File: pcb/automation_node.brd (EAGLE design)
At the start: 107.1 x 77.8 mm, 27 parts, among them IC1 POWER_FET, IC2 POWER_FET, IC3 POWER_FET, IC4 POWER_FET, IC5 POWER_FET, IC6 FEATHER-ESP32, J1 POWER-VIAS, J2 POWER-VIAS, J3 POWER-VIAS, J4 POWER-VIAS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

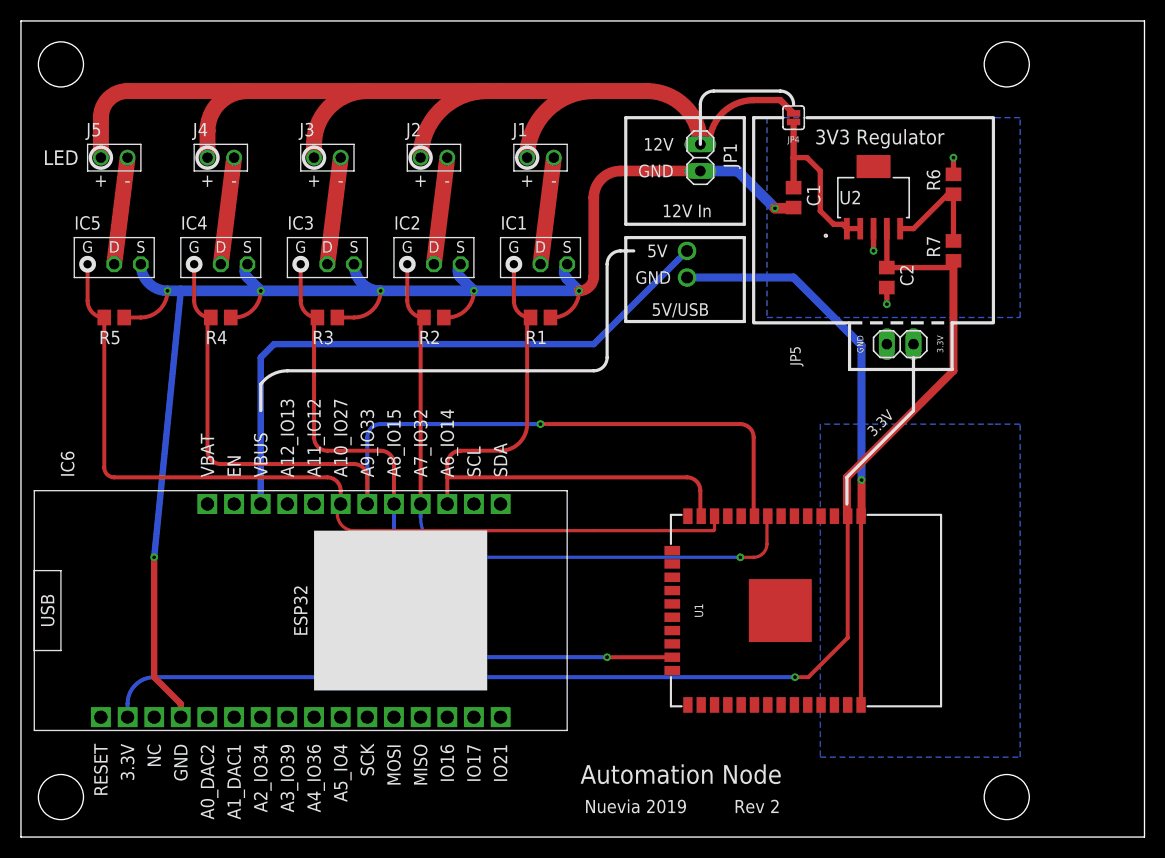
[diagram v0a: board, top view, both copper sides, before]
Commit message: added RFM69, finished routing all but RFM69
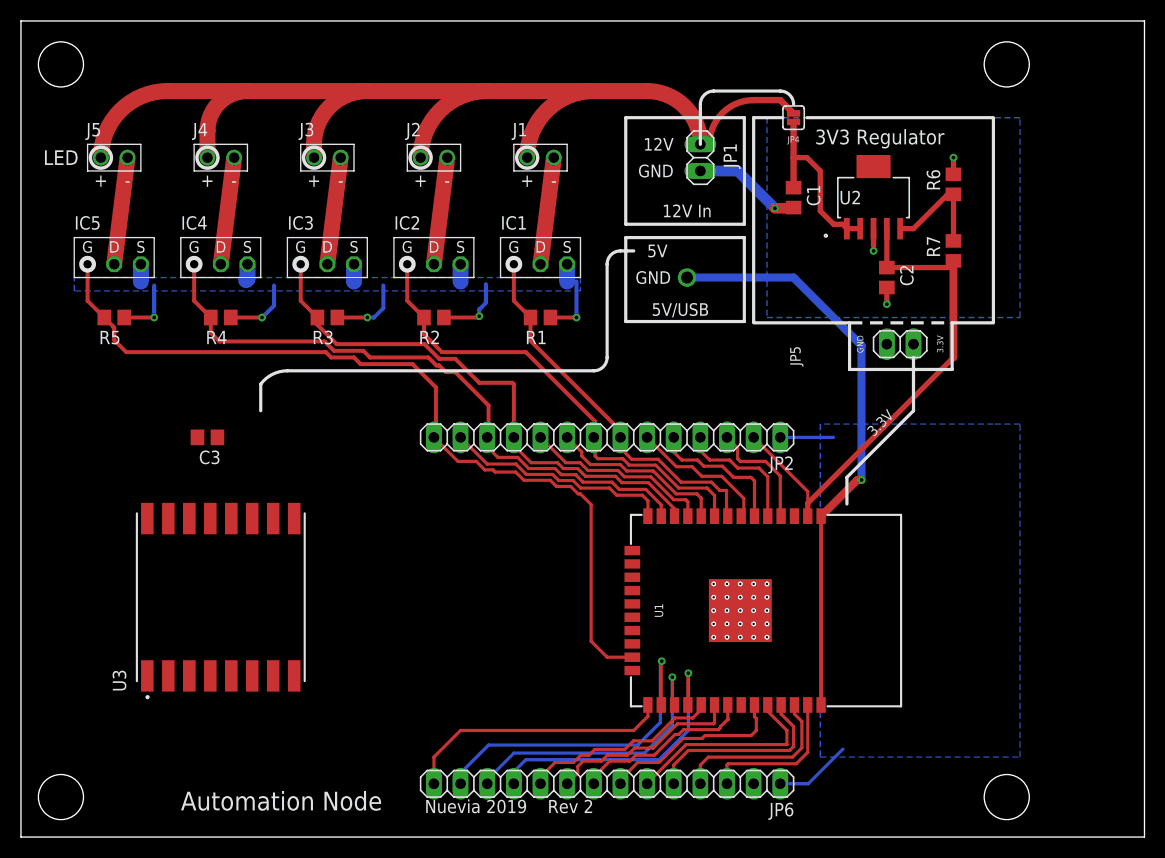
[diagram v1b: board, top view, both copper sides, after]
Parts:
- removed IC6: FEATHER-ESP32, VCO-Eagle_parts:ESP32_FEATHER
- added C3: 100uF, rcl:C0805
- added JP6: (no value), pinhead:1X14
- added U3: RFM69HCW, VanEagleLib:MOD_COM-13909
- JP2: value PROTO_VIA_COMPACT -> (none); device VanEagleLib:PROTO_VIA -> pinhead:1X14
- moved JP2 19.3 mm to (55.9, 38.1), turned to 180 degrees
- moved U1 3.81 mm to (68.6, 21.6)
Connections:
- removed net +5V: IC6.VBUS, JP2.1
- new net ADC1: JP2.3, U1.4
- new net ADC2: JP2.4, U1.5
- new net ADC3: JP2.5, U1.6
- new net ADC4: JP2.6, U1.7
- new net ANT: U3.9
- new net GPIO0: JP6.14, U1.25
- new net IO12: JP2.13, U1.14
- new net IO16: JP6.12, U1.27
- new net IO17: JP6.11, U1.28
- new net IO25: JP2.9, U1.10
- new net IO26: JP2.10, U1.11
- new net MISO: JP6.8, U1.31, U3.2
- new net MOSI: JP6.3, U1.37, U3.3
- new net RFM69_IRQ: JP6.13, U1.26, U3.14
- new net RFM69_RS: U3.6
- new net RFM69_SS: JP6.10, U1.29, U3.5
- new net RX: JP6.6, U1.34
- new net SCK: JP6.9, U1.30, U3.4
- new net SCL: JP6.4, U1.36
- new net SDA: JP6.7, U1.33
- new net TX: JP6.5, U1.35
- net +3V3: now also C3.1, JP2.2, JP6.2, U3.13; no longer IC6.3.3V
- net GND: now also C3.2, JP2.1, JP6.1, U3.1, U3.10, U3.8; no longer IC6.GND
- net PWM1: now also IC4.1, JP2.12, R4.2; no longer IC1.1, IC6.A6_IO14, R1.2
- net PWM2: now also IC1.1, JP2.7, R1.2; no longer IC2.1, IC6.A7_IO32, R2.2
- net PWM3: now also IC5.1, JP2.14, R5.2; no longer IC3.1, IC6.A8_IO15, R3.2
- net PWM4: now also IC2.1, JP2.8, R2.2; no longer IC4.1, IC6.A9_IO33, R4.2
- net PWM5: now also IC3.1, JP2.11, R3.2; no longer IC5.1, IC6.A10_IO27, R5.2
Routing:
- net GND: track 211.8 -> 126.2 mm, vias 11 -> 10
- net +3V3: track 123.3 -> 50.3 mm, vias 1 -> 0
- net +5V: track 58.8 -> 0.00 mm
- net PWM4: track 89.2 -> 45.6 mm, vias 1 -> 0
- net RFM69_IRQ: track 0.00 -> 32.2 mm, vias 0 -> 1
- net PWM5: track 83.3 -> 52.0 mm
- net IO17: track 0.00 -> 27.9 mm, vias 0 -> 1
- net IO16: track 0.00 -> 27.5 mm, vias 0 -> 1
- net PWM2: track 62.7 -> 36.2 mm, vias 1 -> 0
- net GPIO0: track 0.00 -> 25.6 mm
- net IO12: track 0.00 -> 21.8 mm
- net RX: track 0.00 -> 19.4 mm
- net RFM69_SS: track 0.00 -> 19.1 mm
- net SDA: track 0.00 -> 19.0 mm
- net SCK: track 0.00 -> 18.5 mm
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
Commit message: added programming header for ESP32
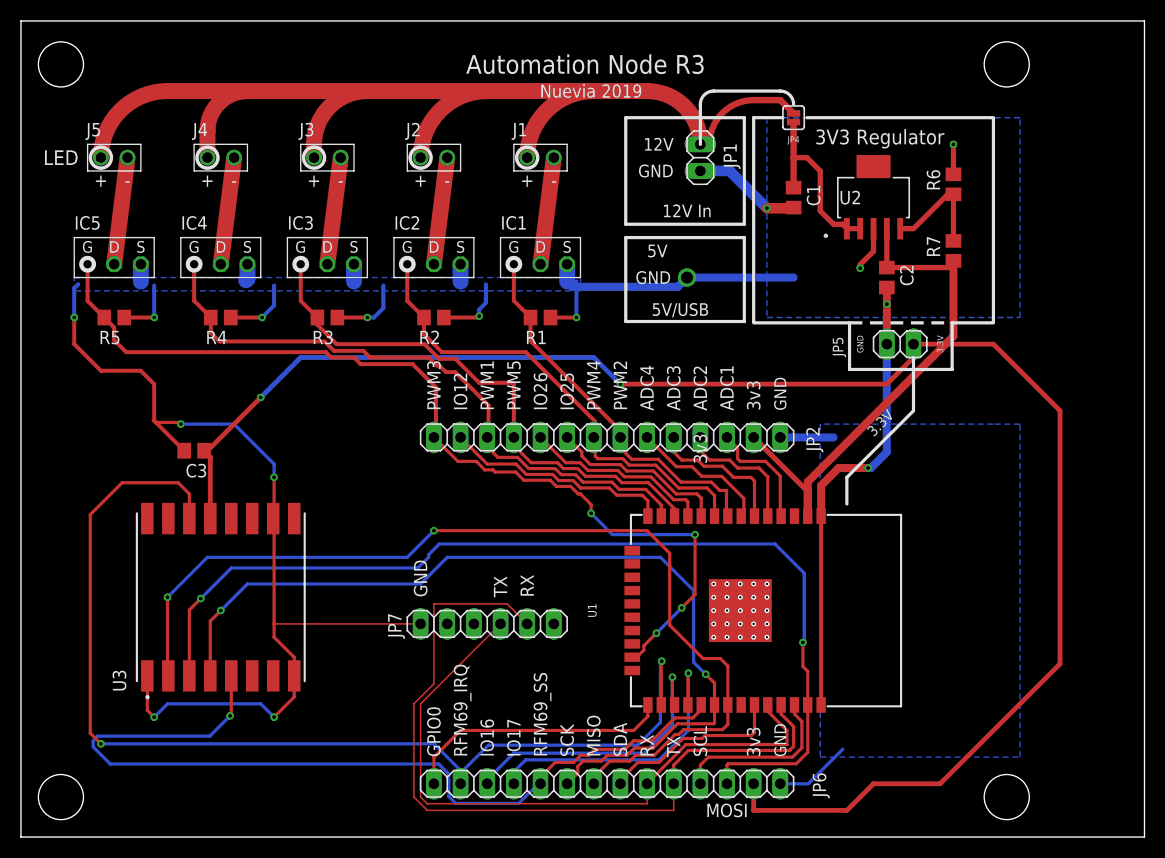
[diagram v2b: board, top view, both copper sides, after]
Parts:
- added JP7: (no value), pinhead:1X06
- moved C3 1.80 mm to (16.5, 36.8)
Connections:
- net GND: now also JP7.1
- net RX: now also JP7.4
- net TX: now also JP7.5
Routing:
- net +3V3: track 50.3 -> 210.0 mm, vias 0 -> 2
- net GND: track 126.2 -> 228.4 mm, vias 10 -> 15
- net MOSI: track 14.5 -> 96.1 mm, vias 0 -> 2
- net MISO: track 17.2 -> 94.0 mm, vias 0 -> 2
- net RFM69_IRQ: track 32.2 -> 104.5 mm, vias 1 -> 2
- net SCK: track 18.5 -> 85.4 mm, vias 0 -> 2
- net RFM69_SS: track 19.1 -> 84.5 mm, vias 0 -> 1
- net TX: track 18.4 -> 75.1 mm
- net RX: track 19.4 -> 62.9 mm
- net PWM3: track 81.0 -> 89.4 mm, vias 0 -> 4
- net SDA: track 19.0 -> 17.6 mm
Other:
- board text added: "3v3"
- board text added: "ADC1"
- board text added: "ADC2"
- board text added: "ADC3"
- board text added: "ADC4"
- board text added: "Automation Node R3"
- board text added: "GPIO0"
- board text added: "IO12"
- board text added: "IO16"
- board text added: "IO17"
- board text added: "IO25"
- board text added: "IO26"
- board text added: "MISO"
- board text added: "MOSI"
- board text added: "PWM1"
- board text added: "PWM2"
- board text added: "PWM3"
- board text added: "PWM4"
- board text added: "PWM5"
- board text added: "RFM69_IRQ"
- board text added: "RFM69_SS"
- board text added: "RX"
- board text added: "SCK"
- board text added: "SCL"
- board text added: "SDA"
- board text added: "TX"
- board text removed: "Automation Node"
- board text removed: "Rev 2"

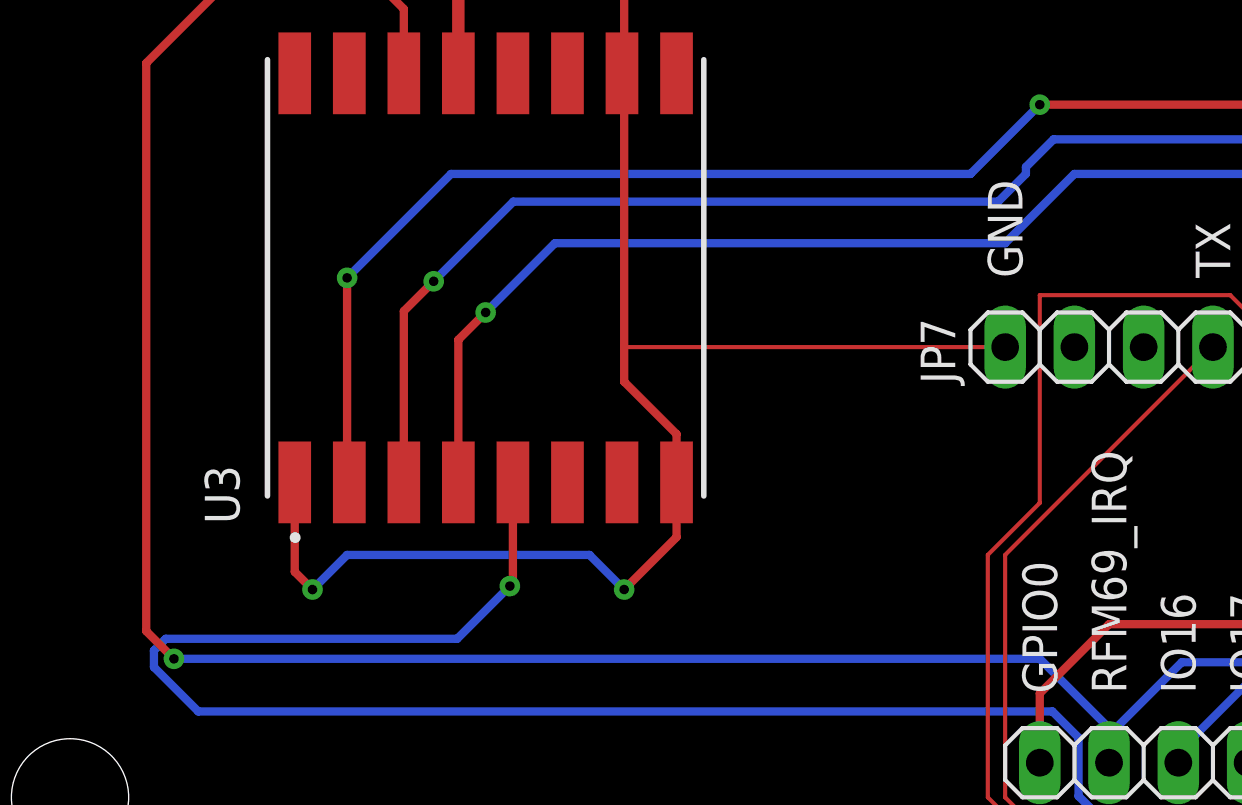
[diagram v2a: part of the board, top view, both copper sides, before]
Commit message: moved vias away from bottom side of rfm69
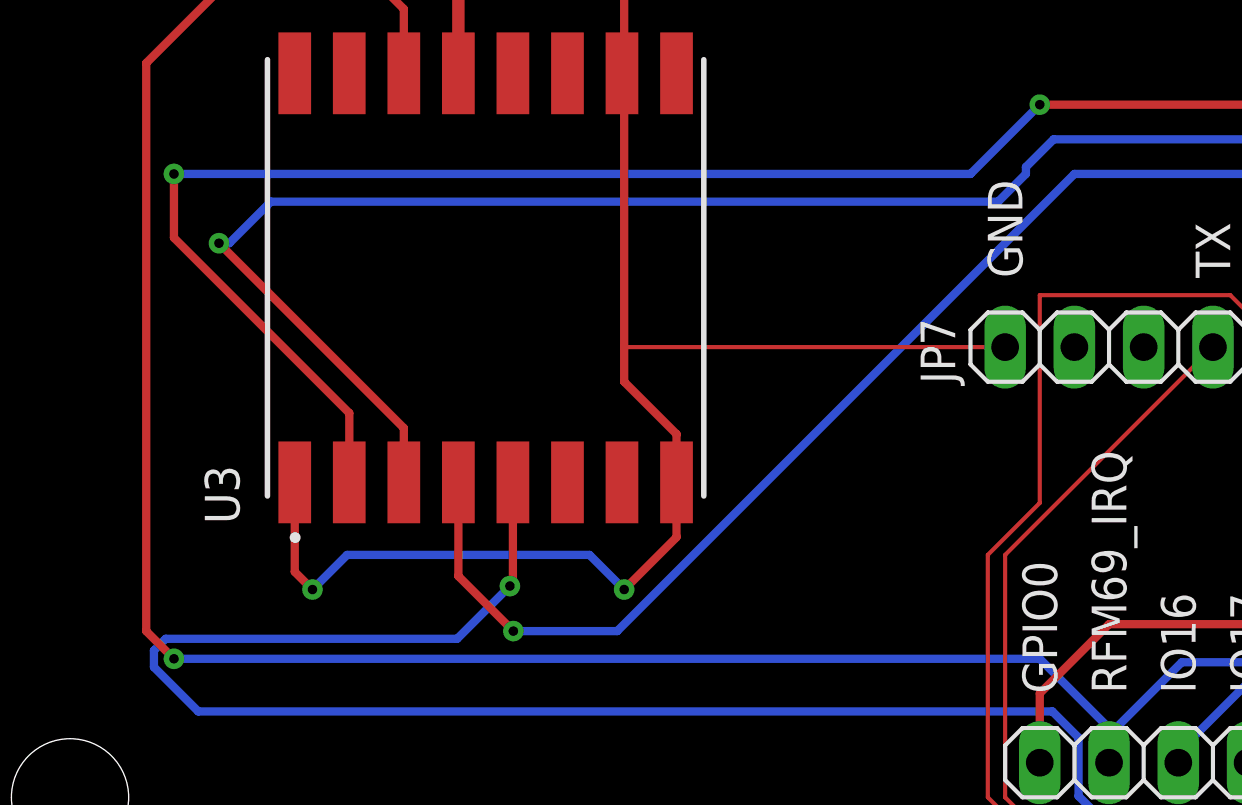
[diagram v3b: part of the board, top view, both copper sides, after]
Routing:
- net MISO: track 94.0 -> 105.2 mm
- net MOSI: track 96.1 -> 107.2 mm
- net SCK: track 85.4 -> 88.9 mm
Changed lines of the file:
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@@
 <setting verticaltext="up"/>
 </settings>
-<grid distance="50" unitdist="mil" unit="mil" style="lines" multiple="1" display="no" altdistance="5" altunitdist="mil" altunit="mil"/>
+<grid distance="50" unitdist="mil" unit="mm" style="lines" multiple="1" display="no" altdistance="5" altunitdist="mil" altunit="mil"/>
 <layers>
 <layer number="1" name="Top" color="4" fill="1" visible="yes" active="yes"/>
@@
 <wire x1="55.90253125" y1="7.7978" x2="57.80753125" y2="7.7978" width="0.3048" layer="1"/>
 <wire x1="58.49333125" y1="8.4836" x2="60.27133125" y2="8.4836" width="0.3048" layer="1"/>
-<wire x1="18.05" y1="15.36" x2="18.05" y2="20.59" width="0.3048" layer="1"/>
-<wire x1="18.05" y1="20.59" x2="19.05" y2="21.59" width="0.3048" layer="1"/>
-<via x="19.05" y="21.59" extent="1-16" drill="0.35"/>
-<wire x1="19.05" y1="21.59" x2="21.59" y2="24.13" width="0.3048" layer="16"/>
-<wire x1="21.59" y1="24.13" x2="38.1" y2="24.13" width="0.3048" layer="16"/>
-<wire x1="38.1" y1="24.13" x2="40.64" y2="26.67" width="0.3048" layer="16"/>
+<wire x1="20.066" y1="9.906" x2="18.05" y2="11.922" width="0.3048" layer="1"/>
+<wire x1="18.05" y1="15.36" x2="18.05" y2="11.922" width="0.3048" layer="1"/>
+<via x="20.066" y="9.906" extent="1-16" drill="0.35"/>
+<wire x1="40.64" y1="26.67" x2="23.876" y2="9.906" width="0.3048" layer="16"/>
+<wire x1="20.066" y1="9.906" x2="23.876" y2="9.906" width="0.3048" layer="16"/>
 <wire x1="40.64" y1="26.67" x2="60.96" y2="26.67" width="0.3048" layer="16"/>
 <wire x1="64.135" y1="16.6652" x2="65.278" y2="15.5222" width="0.3048" layer="16"/>
@@
 <wire x1="67.31" y1="6.858" x2="67.31" y2="5.08" width="0.3048" layer="1"/>
 <wire x1="75.01" y1="8.081" x2="73.914" y2="6.985" width="0.3048" layer="1"/>
-<wire x1="16.05" y1="15.36" x2="16.05" y2="21.638" width="0.3048" layer="1"/>
-<wire x1="16.05" y1="21.638" x2="17.145" y2="22.733" width="0.3048" layer="1"/>
-<via x="17.145" y="22.733" extent="1-16" drill="0.35"/>
-<wire x1="17.145" y1="22.733" x2="20.066" y2="25.654" width="0.3048" layer="16"/>
-<wire x1="20.066" y1="25.654" x2="37.846" y2="25.654" width="0.3048" layer="16"/>
+<wire x1="16.05" y1="15.36" x2="16.05" y2="17.351" width="0.3048" layer="1"/>
+<wire x1="16.05" y1="17.351" x2="9.271" y2="24.13" width="0.3048" layer="1"/>
+<via x="9.271" y="24.13" extent="1-16" drill="0.35"/>
+<wire x1="11.176" y1="25.654" x2="9.652" y2="24.13" width="0.3048" layer="16"/>
+<wire x1="9.271" y1="24.13" x2="9.652" y2="24.13" width="0.3048" layer="16"/>
+<wire x1="11.176" y1="25.654" x2="37.846" y2="25.654" width="0.3048" layer="16"/>
 <wire x1="37.846" y1="25.654" x2="38.862" y2="26.67" width="0.3048" layer="16"/>
 <wire x1="38.862" y1="26.67" x2="38.862" y2="26.924" width="0.3048" layer="16"/>
@@
 <wire x1="60.3758" y1="7.7978" x2="58.5978" y2="7.7978" width="0.3048" layer="1"/>
 <wire x1="58.5978" y1="7.7978" x2="58.039" y2="7.239" width="0.3048" layer="1"/>
-<wire x1="14.05" y1="15.36" x2="13.97" y2="15.44" width="0.3048" layer="1"/>
-<wire x1="13.97" y1="15.44" x2="13.97" y2="22.86" width="0.3048" layer="1"/>
-<via x="13.97" y="22.86" extent="1-16" drill="0.35"/>
-<wire x1="13.97" y1="22.86" x2="17.78" y2="26.67" width="0.3048" layer="16"/>
-<wire x1="17.78" y1="26.67" x2="36.83" y2="26.67" width="0.3048" layer="16"/>
+<wire x1="14.05" y1="15.36" x2="14.05" y2="17.9" width="0.3048" layer="1"/>
+<wire x1="7.62" y1="26.67" x2="7.62" y2="24.33" width="0.3048" layer="1"/>
+<wire x1="14.05" y1="17.9" x2="7.62" y2="24.33" width="0.3048" layer="1"/>
+<via x="7.62" y="26.67" extent="1-16" drill="0.35"/>
+<wire x1="7.62" y1="26.67" x2="36.83" y2="26.67" width="0.3048" layer="16"/>
 <wire x1="36.83" y1="26.67" x2="39.37" y2="29.21" width="0.3048" layer="16"/>
 <wire x1="39.37" y1="29.21" x2="59.69" y2="29.21" width="0.3048" layer="1"/>

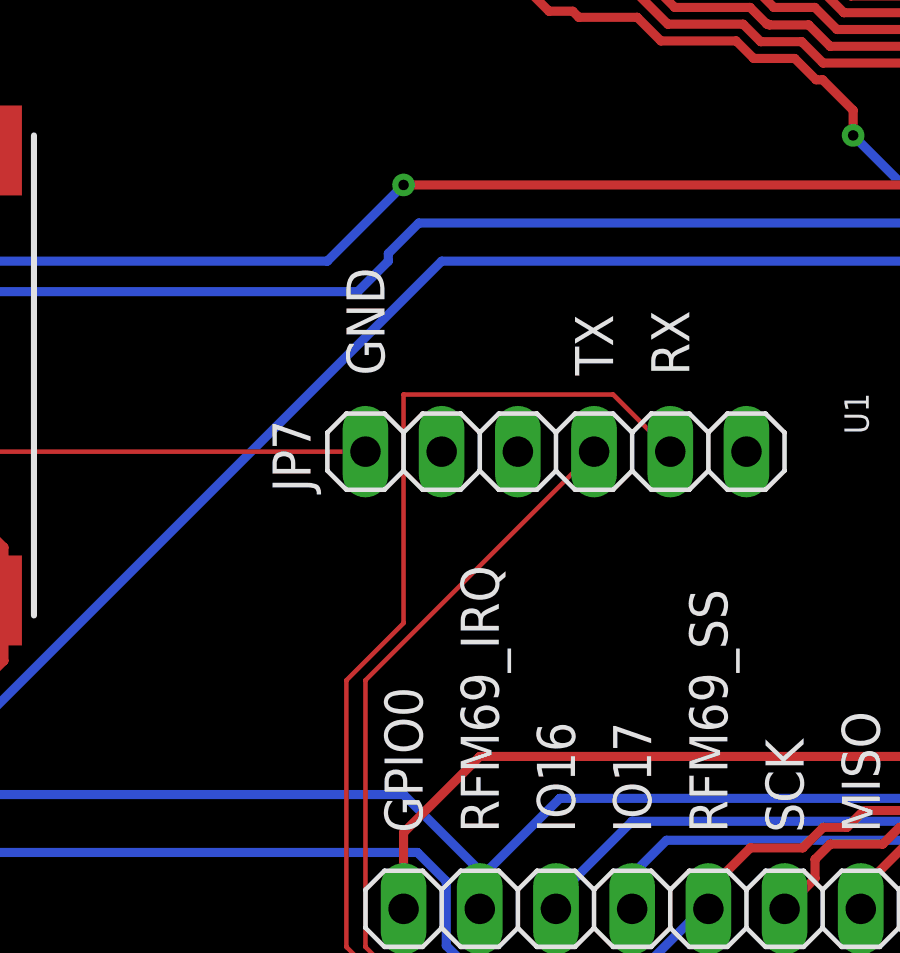
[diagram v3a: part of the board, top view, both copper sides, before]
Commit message: added GPIO0 to programming header
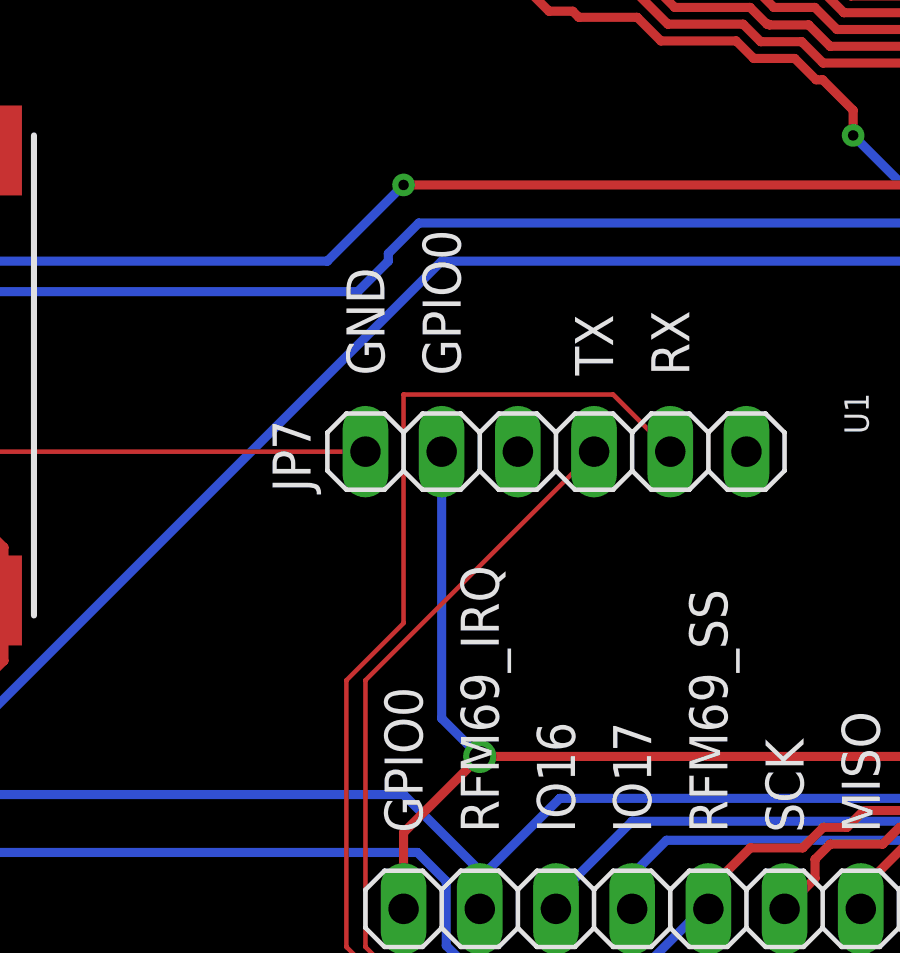
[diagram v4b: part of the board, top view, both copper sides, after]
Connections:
- net GPIO0: now also JP7.2
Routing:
- net GPIO0: track 25.6 -> 36.3 mm, vias 0 -> 1
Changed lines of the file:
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@@
 <text x="48.26" y="22.86" size="1.27" layer="21" rot="R270" align="center-right">RX</text>
 <text x="45.72" y="22.86" size="1.27" layer="21" rot="R270" align="center-right">TX</text>
+<text x="40.64" y="22.86" size="1.27" layer="21" rot="R270" align="center-right">GPIO0</text>
 </plain>
 <attributes>
@@
 <wire x1="58.42" y1="10.16" x2="59.77" y2="11.51" width="0.3048" layer="1"/>
 <wire x1="59.77" y1="11.51" x2="59.77" y2="12.59" width="0.3048" layer="1"/>
+<contactref element="JP7" pad="2"/>
+<wire x1="40.64" y1="11.43" x2="41.91" y2="10.16" width="0.3048" layer="16"/>
+<via x="41.91" y="10.16" extent="1-16" drill="0.7"/>
+<wire x1="40.64" y1="20.32" x2="40.64" y2="11.43" width="0.3048" layer="16"/>
 </signal>
 <signal name="RFM69_IRQ">
